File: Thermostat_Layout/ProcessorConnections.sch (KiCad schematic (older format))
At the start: 17 parts, among them J1 Conn_01x03, J2 Conn_01x03, SW1 SW_Push, U1 LM50CIM3, U2 ATMEGA328P-AU, Y1 Crystal

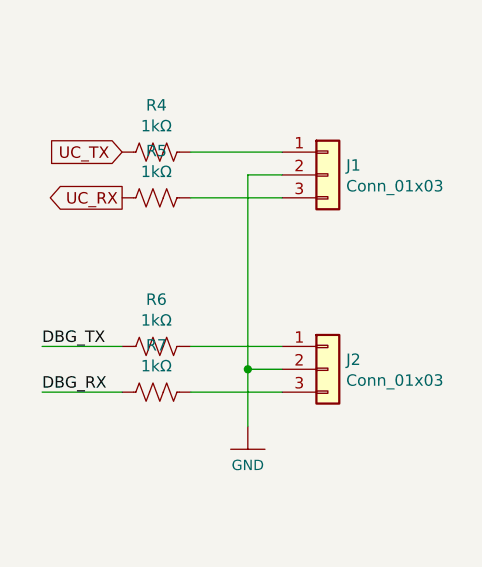
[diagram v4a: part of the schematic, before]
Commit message: Schematic and PCB layout for thermostat
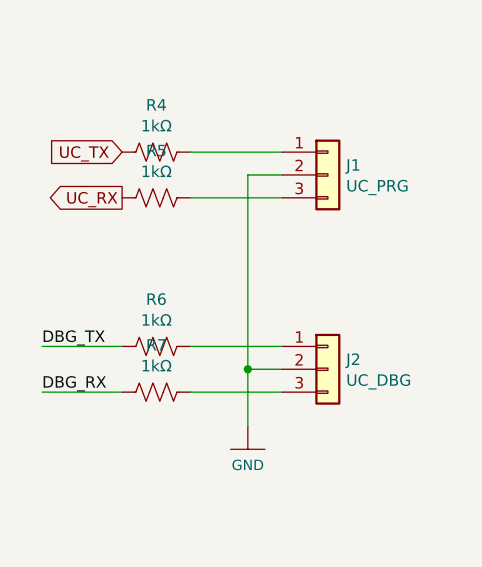
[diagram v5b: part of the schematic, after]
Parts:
- J1: value Conn_01x03 -> UC_PRG; footprint Connector_JST:JST_PH_S3B-PH-SM4-TB_1x03-1MP_P2.00mm_Horizontal -> Connector_JST:JST_EH_B3B-EH-A_1x03_P2.50mm_Vertical
- J2: value Conn_01x03 -> UC_DBG; footprint Connector_JST:JST_PH_S3B-PH-SM4-TB_1x03-1MP_P2.00mm_Horizontal -> Connector_JST:JST_EH_B3B-EH-A_1x03_P2.50mm_Vertical
- Y1: footprint Crystal:Crystal_SMD_SeikoEpson_MC405-2Pin_9.6x4.1mm -> Crystal:Crystal_SMD_0603-2Pin_6.0x3.5mm_HandSoldering
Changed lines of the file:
@@
 	5200 4050 5200 4100
-$Comp
-L Device:R_US R1
-U 1 1 5D431858
-P 1950 1350
-F 0 "R1" H 2018 1396 50  0000 L CNN
-F 1 "4.7K" H 2018 1305 50  0000 L CNN
-F 2 "Resistor_SMD:R_0402_1005Metric" V 1990 1340 50  0001 C CNN
-F 3 "~" H 1950 1350 50  0001 C CNN
-	1    1950 1350
-	1    0    0    -1
-$EndComp
 $Comp
 L Device:R_US R2
@@
 P 9400 1600
 F 0 "J1" H 9480 1642 50  0000 L CNN
-F 1 "Conn_01x03" H 9480 1551 50  0000 L CNN
-F 2 "Connector_JST:JST_PH_S3B-PH-SM4-TB_1x03-1MP_P2.00mm_Horizontal" H 9400 1600 50  0001 C CNN
+F 1 "UC_PRG" H 9480 1551 50  0000 L CNN
+F 2 "Connector_JST:JST_EH_B3B-EH-A_1x03_P2.50mm_Vertical" H 9400 1600 50  0001 C CNN
 F 3 "~" H 9400 1600 50  0001 C CNN
 	1    9400 1600
@@
 	1    0    0    -1
 $EndComp
-$Comp
-L Device:Crystal Y1
-U 1 1 5D476A0F
-P 2000 2650
-F 0 "Y1" H 2000 2918 50  0000 C CNN
-F 1 "Crystal" H 2000 2827 50  0000 C CNN
-F 2 "Crystal:Crystal_SMD_SeikoEpson_MC405-2Pin_9.6x4.1mm" H 2000 2650 50  0001 C CNN
-F 3 "~" H 2000 2650 50  0001 C CNN
-	1    2000 2650
-	1    0    0    -1
-$EndComp
 Text GLabel 5000 2550 0    50   Input ~ 0
 RADIO_STATUS
@@
 P 9400 2450
 F 0 "J2" H 9480 2492 50  0000 L CNN
-F 1 "Conn_01x03" H 9480 2401 50  0000 L CNN
-F 2 "Connector_JST:JST_PH_S3B-PH-SM4-TB_1x03-1MP_P2.00mm_Horizontal" H 9400 2450 50  0001 C CNN
+F 1 "UC_DBG" H 9480 2401 50  0000 L CNN
+F 2 "Connector_JST:JST_EH_B3B-EH-A_1x03_P2.50mm_Vertical" H 9400 2450 50  0001 C CNN
 F 3 "~" H 9400 2450 50  0001 C CNN
 	1    9400 2450
@@
 Text Label 8150 2550 0    50   ~ 0
 DBG_RX
+$Comp
+L Device:R_US R1
+U 1 1 5D431858
+P 1950 1350
+F 0 "R1" H 2018 1396 50  0000 L CNN
+F 1 "4.7K" H 2018 1305 50  0000 L CNN
+F 2 "Resistor_SMD:R_0402_1005Metric" V 1990 1340 50  0001 C CNN
+F 3 "~" H 1950 1350 50  0001 C CNN
+	1    1950 1350
+	1    0    0    -1
+$EndComp
+$Comp
+L Device:Crystal Y1
+U 1 1 5D476A0F
+P 2000 2650
+F 0 "Y1" H 2000 2918 50  0000 C CNN
+F 1 "Crystal" H 2000 2827 50  0000 C CNN
+F 2 "Crystal:Crystal_SMD_0603-2Pin_6.0x3.5mm_HandSoldering" H 2000 2650 50  0001 C CNN
+F 3 "~" H 2000 2650 50  0001 C CNN
+	1    2000 2650
+	1    0    0    -1
+$EndComp
 $EndSCHEMATC
